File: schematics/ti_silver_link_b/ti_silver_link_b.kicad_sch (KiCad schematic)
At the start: 40 parts, among them P1 Conn_1x5, U1 24LC64, U2 TPS71533__SC70, U3 TUSB3410, U4 IMH8A, Y1 12MHz

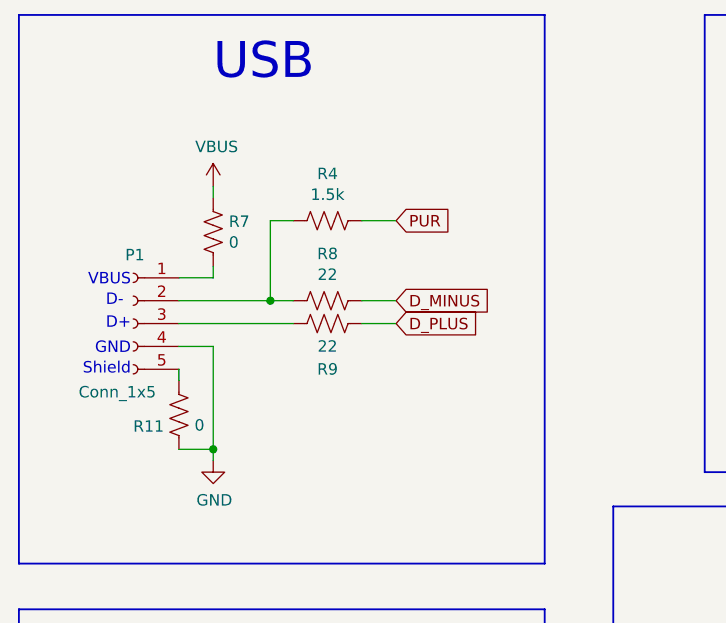
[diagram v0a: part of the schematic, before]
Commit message: Correct "B" and "okrayo" PUR resistor connection to D+
Rev 1 schematic incorrectly identified PUR resistor connection to D- and
had the series resistors for D+/D- (R8/R9) swapped. Move PUR resistor R4
to D+ and use R8 for D+ and R9 for D-.
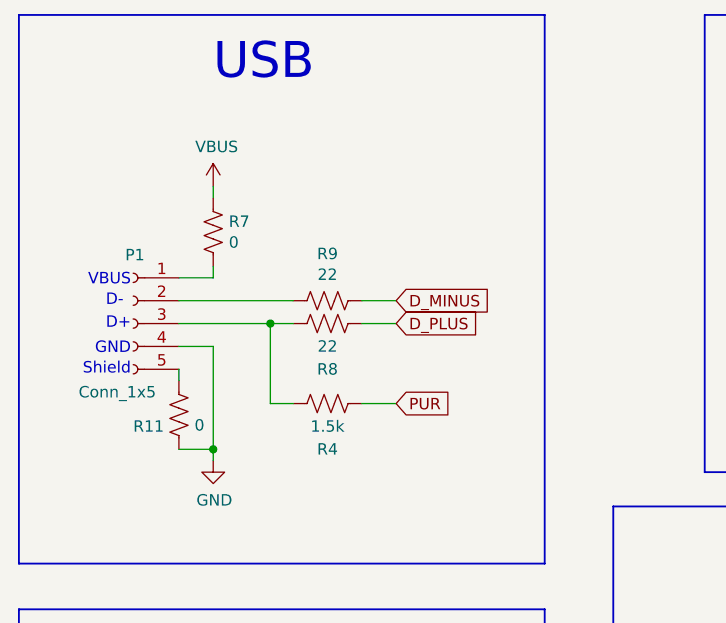
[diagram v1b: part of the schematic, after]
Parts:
- renumbered R9 to R8, R8 to R9
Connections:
- net at P1.2 (Pin_2), R9.2: no longer R4.2
- net at P1.3 (Pin_3), R8.2: now also R4.2
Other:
- title: TI Silver Link "B" -> TI Silver Graph Link "B"
- moved on the sheet: R4

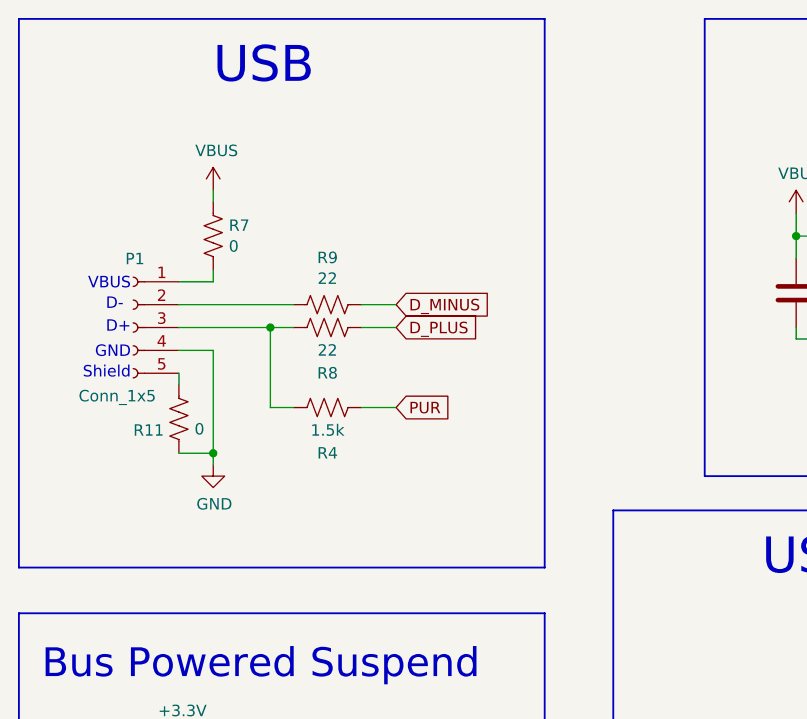
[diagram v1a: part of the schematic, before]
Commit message: Add no-stuff C8 and C11 on "B" Schematic
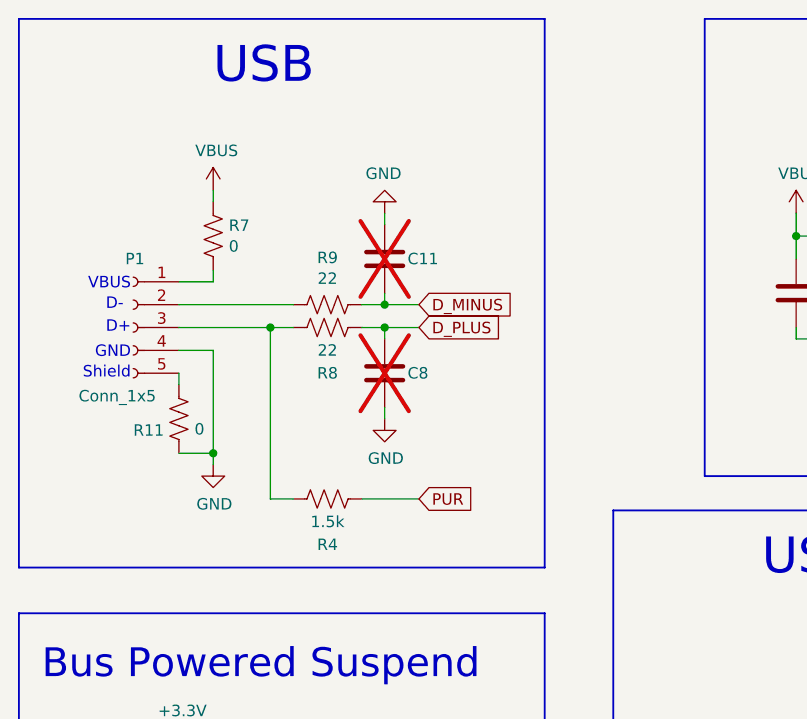
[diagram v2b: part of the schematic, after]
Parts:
- added C11, C8: ~, symbol Device:C
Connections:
- net D_MINUS: now also C11.2
- net D_PLUS: now also C8.1
- net GND: now also C11.1, C8.2
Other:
- moved on the sheet: R4
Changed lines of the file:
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@@
   (junction (at 114.3 139.7) (diameter 0) (color 0 0 0 0)
   )
+  (junction (at 76.2 52.07) (diameter 0) (color 0 0 0 0)
+  )
   (junction (at 63.5 54.61) (diameter 0) (color 0 0 0 0)
   )
@@
   )
   (junction (at 227.33 64.77) (diameter 0) (color 0 0 0 0)
+  )
+  (junction (at 76.2 54.61) (diameter 0) (color 0 0 0 0)
   )
   (junction (at 149.86 154.94) (diameter 0) (color 0 0 0 0)
@@
     (stroke (width 0) (type default))
   )
-  (wire (pts (xy 73.66 54.61) (xy 77.47 54.61))
+  (wire (pts (xy 73.66 54.61) (xy 76.2 54.61))
     (stroke (width 0) (type default))
   )
@@
     (stroke (width 0) (type default))
   )
+  (wire (pts (xy 76.2 63.5) (xy 76.2 64.77))
+    (stroke (width 0) (type default))
+  )
   (wire (pts (xy 227.33 41.91) (xy 227.33 40.64))
     (stroke (width 0) (type default))
@@
     (stroke (width 0) (type default))
   )
+  (wire (pts (xy 76.2 50.8) (xy 76.2 52.07))
+    (stroke (width 0) (type default))
+  )
   (wire (pts (xy 121.92 54.61) (xy 121.92 55.88))
     (stroke (width 0) (type default))
@@
     (stroke (width 0) (type default))
   )
+  (wire (pts (xy 76.2 54.61) (xy 80.01 54.61))
+    (stroke (width 0) (type default))
+  )
   (wire (pts (xy 60.96 160.02) (xy 60.96 158.75))
     (stroke (width 0) (type default))
@@
     (stroke (width 0.2032) (type solid))
   )
-  (wire (pts (xy 66.04 63.5) (xy 63.5 63.5))
+  (wire (pts (xy 66.04 73.66) (xy 63.5 73.66))
     (stroke (width 0) (type default))
   )
@@
     (stroke (width 0.2032) (type solid))
   )
+  (wire (pts (xy 76.2 52.07) (xy 80.01 52.07))
+    (stroke (width 0) (type default))
+  )
   (wire (pts (xy 53.34 160.02) (xy 53.34 158.75))
     (stroke (width 0) (type default))
@@
     (stroke (width 0) (type default))
   )
-  (wire (pts (xy 73.66 52.07) (xy 77.47 52.07))
+  (wire (pts (xy 73.66 52.07) (xy 76.2 52.07))
     (stroke (width 0) (type default))
   )
@@
     (stroke (width 0) (type default))
   )
+  (wire (pts (xy 76.2 54.61) (xy 76.2 55.88))
+    (stroke (width 0) (type default))
+  )
   (wire (pts (xy 66.04 118.11) (xy 64.77 118.11))
     (stroke (width 0) (type default))
@@
     (stroke (width 0) (type default))
   )
+  (wire (pts (xy 76.2 41.91) (xy 76.2 43.18))
+    (stroke (width 0) (type default))
+  )
   (polyline (pts (xy 250.19 93.98) (xy 205.74 93.98))
     (stroke (width 0.2032) (type solid))
@@
     (stroke (width 0) (type default))
   )
-  (wire (pts (xy 63.5 54.61) (xy 63.5 63.5))
+  (wire (pts (xy 63.5 54.61) (xy 63.5 73.66))
     (stroke (width 0) (type default))
   )
@@
     (stroke (width 0) (type default))
   )
-  (wire (pts (xy 73.66 63.5) (xy 77.47 63.5))
+  (wire (pts (xy 73.66 73.66) (xy 80.01 73.66))
     (stroke (width 0) (type default))
   )
@@
     )
   )
-  (global_label "PUR" (shape input) (at 77.47 63.5 0)
+  (global_label "PUR" (shape input) (at 80.01 73.66 0)
     (effects (font (size 1.27 1.27)) (justify left))
-    (property "Intersheetrefs" "${INTERSHEET_REFS}" (at 77.47 63.5 0)
+    (property "Intersheetrefs" "${INTERSHEET_REFS}" (at 80.01 73.66 0)
       (effects (font (size 1.27 1.27)) hide)
     )
@@
     )
   )
-  (global_label "D_MINUS" (shape input) (at 77.47 52.07 0)
+  (global_label "D_MINUS" (shape input) (at 80.01 52.07 0)
     (effects (font (size 1.27 1.27)) (justify left))
-    (property "Intersheetrefs" "${INTERSHEET_REFS}" (at 77.47 52.07 0)
-      (effects (font (size 1.27 1.27)) hide)
-    )
-  )
-  (global_label "D_PLUS" (shape input) (at 77.47 54.61 0)
+    (property "Intersheetrefs" "${INTERSHEET_REFS}" (at 80.01 52.07 0)
+      (effects (font (size 1.27 1.27)) hide)
+    )
+  )
+  (global_label "D_PLUS" (shape input) (at 80.01 54.61 0)
     (effects (font (size 1.27 1.27)) (justify left))
-    (property "Intersheetrefs" "${INTERSHEET_REFS}" (at 77.47 54.61 0)
+    (property "Intersheetrefs" "${INTERSHEET_REFS}" (at 80.01 54.61 0)
       (effects (font (size 1.27 1.27)) hide)
     )
@@
     )
   )
-  (symbol (lib_id "Device:R_US") (at 69.85 63.5 270) (unit 1)
-    (in_bom yes) (on_board yes) (dnp no)
-    (property "Reference" "R4" (at 69.85 68.58 90)
-      (effects (font (size 1.27 1.27)))
-    )
-    (property "Value" "1.5k" (at 69.85 66.04 90)
-      (effects (font (size 1.27 1.27)))
-    )
-    (property "Footprint" "" (at 69.596 64.516 90)
-      (effects (font (size 1.27 1.27)) hide)
-    )
-    (property "Datasheet" "~" (at 69.85 63.5 0)
+  (symbol (lib_id "Device:R_US") (at 69.85 73.66 270) (unit 1)
+    (in_bom yes) (on_board yes) (dnp no)
+    (property "Reference" "R4" (at 69.85 78.74 90)
+      (effects (font (size 1.27 1.27)))
+    )
+    (property "Value" "1.5k" (at 69.85 76.2 90)
+      (effects (font (size 1.27 1.27)))
+    )
+    (property "Footprint" "" (at 69.596 74.676 90)
+      (effects (font (size 1.27 1.27)) hide)
+    )
+    (property "Datasheet" "~" (at 69.85 73.66 0)
       (effects (font (size 1.27 1.27)) hide)
     )
@@
         )
       )
+    )
+  )
+  (symbol (lib_id "Device:C") (at 76.2 46.99 0) (unit 1)
+    (in_bom yes) (on_board yes) (dnp yes)
+    (property "Reference" "C11" (at 78.74 46.99 0)
+      (effects (font (size 1.27 1.27)) (justify left))
+    )
+    (property "Value" "~" (at 79.121 48.133 0)
+      (effects (font (size 1.27 1.27)) (justify left))
+    )
+    (property "Footprint" "" (at 77.1652 50.8 0)
+      (effects (font (size 1.27 1.27)) hide)
+    )
+    (property "Datasheet" "~" (at 76.2 46.99 0)
+      (effects (font (size 1.27 1.27)) hide)
+    )
+    (pin "1")
+    (pin "2")
+    (instances
+      (project "ti_silver_link_b"
+        (path "/e5c7f7c6-d5df-4ea5-b677-71f6c803368e"
+          (reference "C11") (unit 1)
+        )
+      )
+    )
+  )
+  (symbol (lib_id "Device:C") (at 76.2 59.69 0) (unit 1)
+    (in_bom yes) (on_board yes) (dnp yes)
+    (property "Reference" "C8" (at 78.74 59.69 0)
+      (effects (font (size 1.27 1.27)) (justify left))
+    )
+    (property "Value" "~" (at 79.121 60.833 0)
+      (effects (font (size 1.27 1.27)) (justify left))
+    )
+    (property "Footprint" "" (at 77.1652 63.5 0)
+      (effects (font (size 1.27 1.27)) hide)
+    )
+    (property "Datasheet" "~" (at 76.2 59.69 0)
+      (effects (font (size 1.27 1.27)) hide)
+    )
+    (pin "1")
+    (pin "2")
+    (instances
+      (project "ti_silver_link_b"
+        (path "/e5c7f7c6-d5df-4ea5-b677-71f6c803368e"
+          (reference "C8") (unit 1)
+        )
+      )
+    )
+  )
+  (symbol (lib_id "power:GND") (at 76.2 64.77 0) (unit 1)
+    (in_bom yes) (on_board yes) (dnp no)
+    (property "Reference" "#PWR02" (at 76.2 71.12 0)
+      (effects (font (size 1.27 1.27)) hide)
+    )
+    (property "Value" "GND" (at 76.327 69.1642 0)
+      (effects (font (size 1.27 1.27)))
+    )
+    (property "Footprint" "" (at 76.2 64.77 0)
+      (effects (font (size 1.27 1.27)) hide)
+    )
+    (property "Datasheet" "" (at 76.2 64.77 0)
+      (effects (font (size 1.27 1.27)) hide)
+    )
+    (pin "1")
+    (instances
+      (project "ti_silver_link_b"
+        (path "/e5c7f7c6-d5df-4ea5-b677-71f6c803368e"
+          (reference "#PWR02") (unit 1)
+        )
+      )
+    )
+  )
+  (symbol (lib_id "power:GND") (at 76.2 41.91 180) (unit 1)
+    (in_bom yes) (on_board yes) (dnp no)
+    (property "Reference" "#PWR01" (at 76.2 35.56 0)
+      (effects (font (size 1.27 1.27)) hide)
+    )
+    (property "Value" "GND" (at 76.073 37.5158 0)
+      (effects (font (size 1.27 1.27)))
+    )
+    (property "Footprint" "" (at 76.2 41.91 0)
+      (effects (font (size 1.27 1.27)) hide)
+    )
+    (property "Datasheet" "" (at 76.2 41.91 0)
+      (effects (font (size 1.27 1.27)) hide)
+    )
+    (pin "1")
+    (instances
+      (project "ti_silver_link_b"
+        (path "/e5c7f7c6-d5df-4ea5-b677-71f6c803368e"
+          (reference "#PWR01") (unit 1)
+        )
+      )

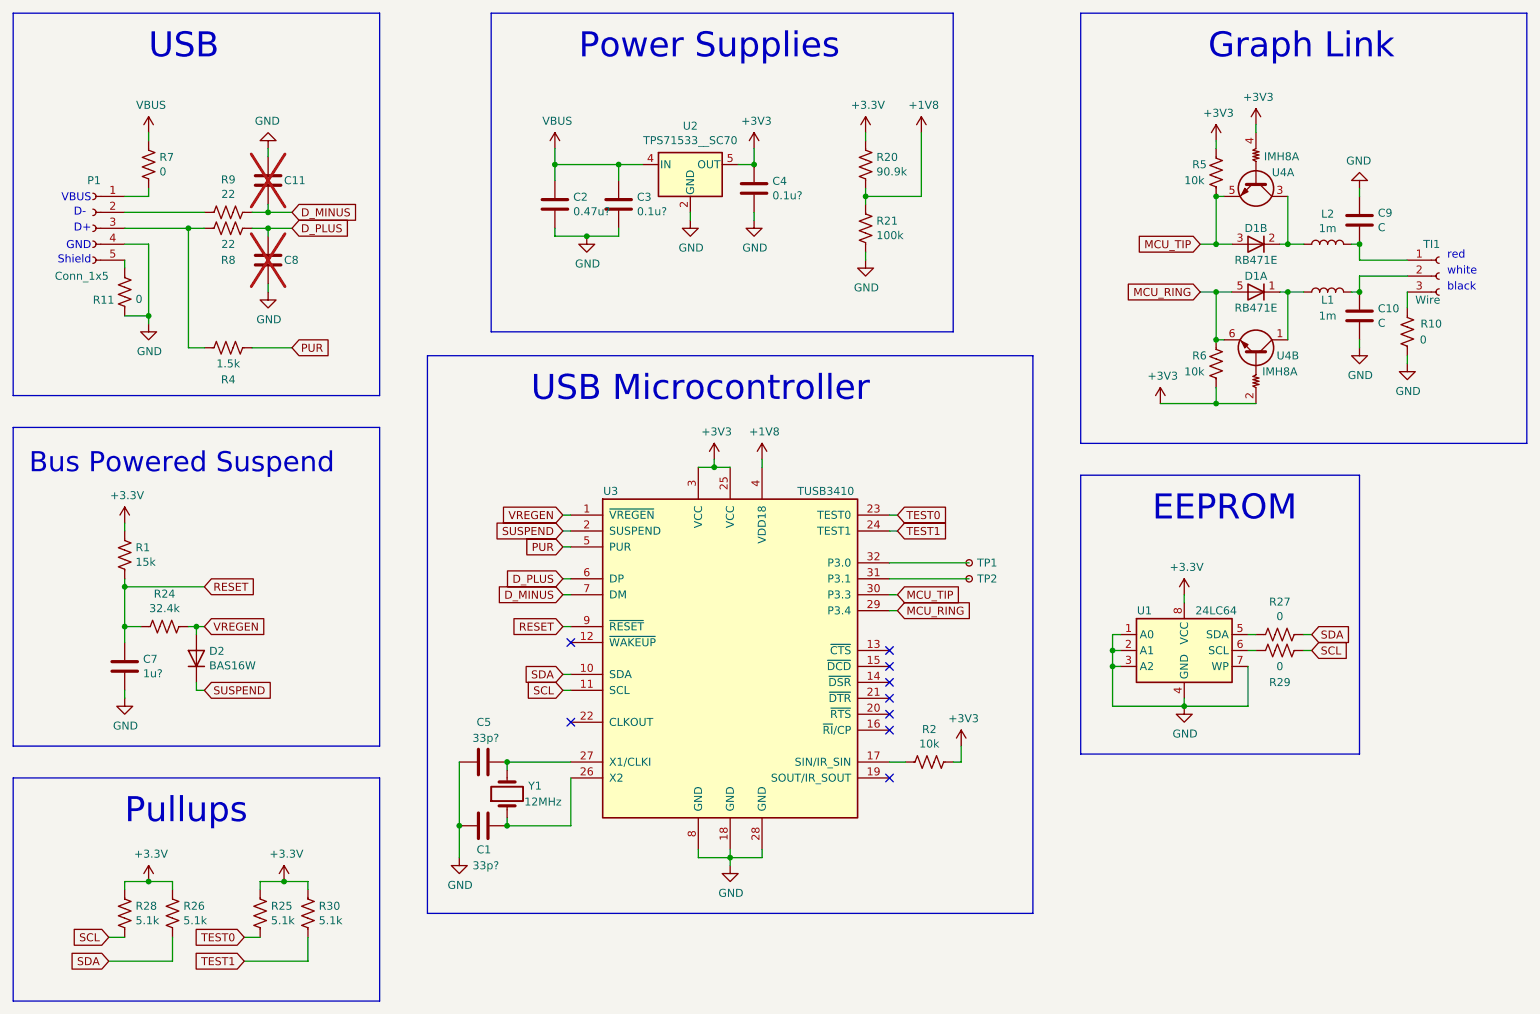
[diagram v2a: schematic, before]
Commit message: Update symbol and datasheet for CH461FGP on "B" schematic
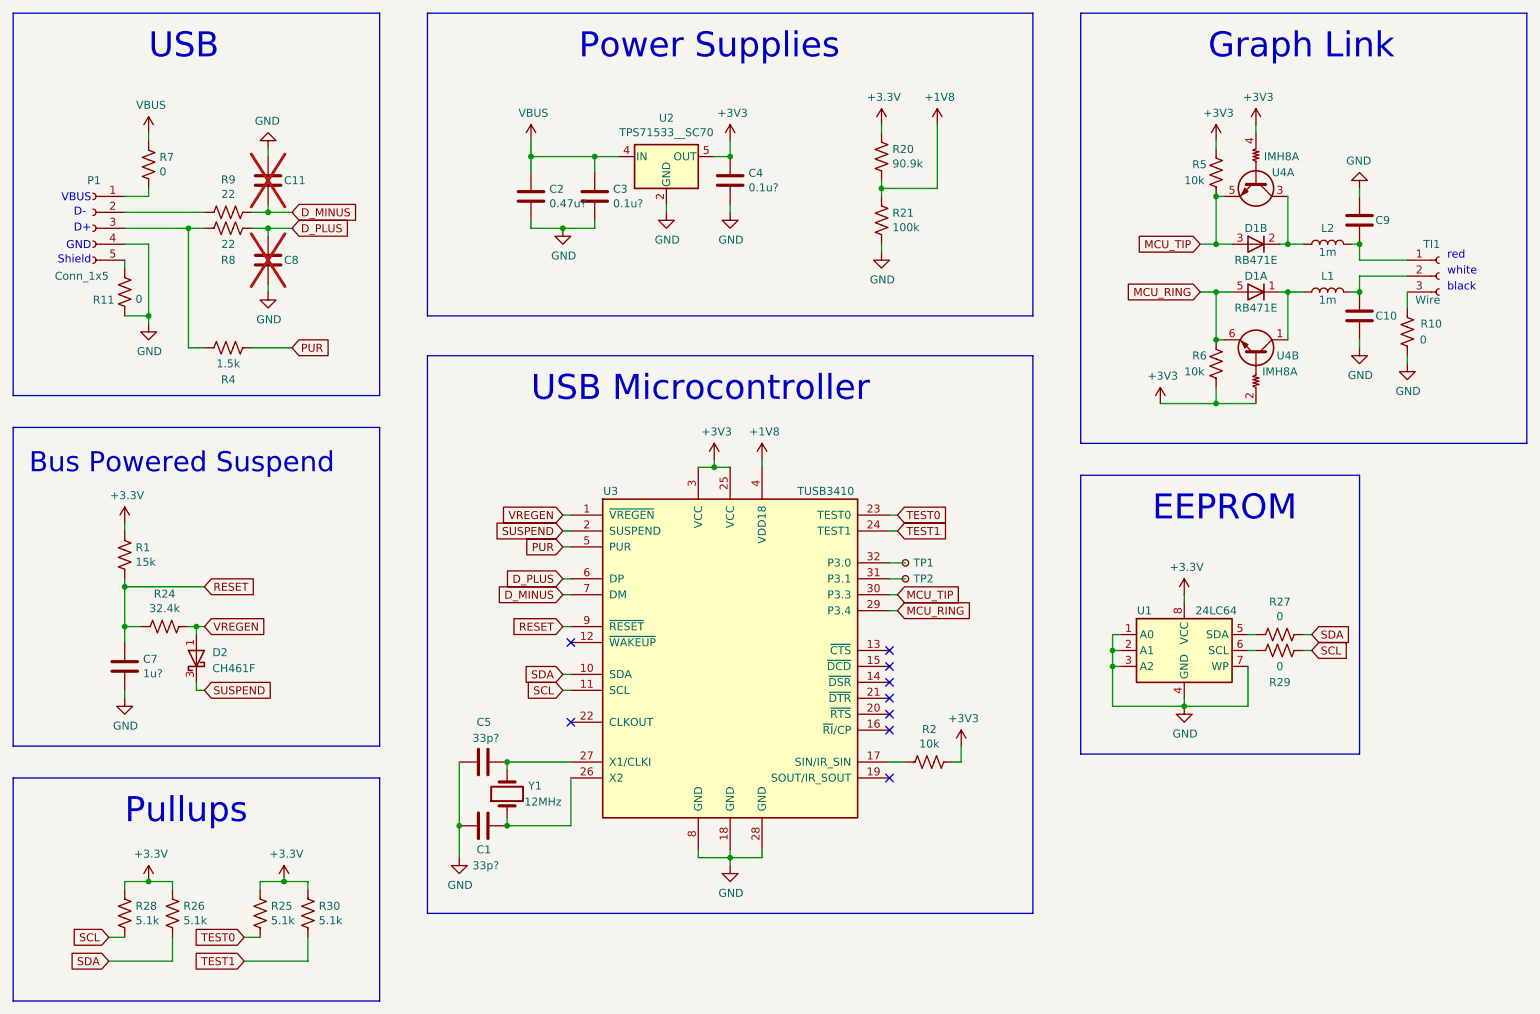
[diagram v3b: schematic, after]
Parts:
- removed D2: BAS16W, Package_TO_SOT_SMD:SOT-323_SC-70, symbol Diode:BAS16W
- added D2: CH461F, Package_TO_SOT_SMD:SOT-323_SC-70, symbol Diode:CH461F
- C10, C9: value C -> ~
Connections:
- net SUSPEND: now also D2.3 (K)
- net VREGEN: now also D2.1 (A)
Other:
- moved on the sheet: C2, C3, C4, R20, R21, TP1, TP2, U2
